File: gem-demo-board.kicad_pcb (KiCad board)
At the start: 6 copper layers, 56 x 66 mm, 153 parts, among them J1 3220-10-0100-00, J10 0473460001, J2 DF13A-2P-1.25H, J3 3220-10-0100-00, J4 2x20_Header_Female, J5 0473460001, J6 556500488, J7 556500488, J8 WE_686115148922_FLIPPED, J9 WE_686115148922_FLIPPED, U1 MCP1700T-3302E_TT, U2 NTS0104BQ, U3 NTS0104BQ, U4 NTS0104BQ, U5 93LC56CT-IMC, U6 FT4232HQ, U7 NTB0104BQ, U8 NTB0104BQ, Y1 ASFLMB-12.000MHZ-LC-T

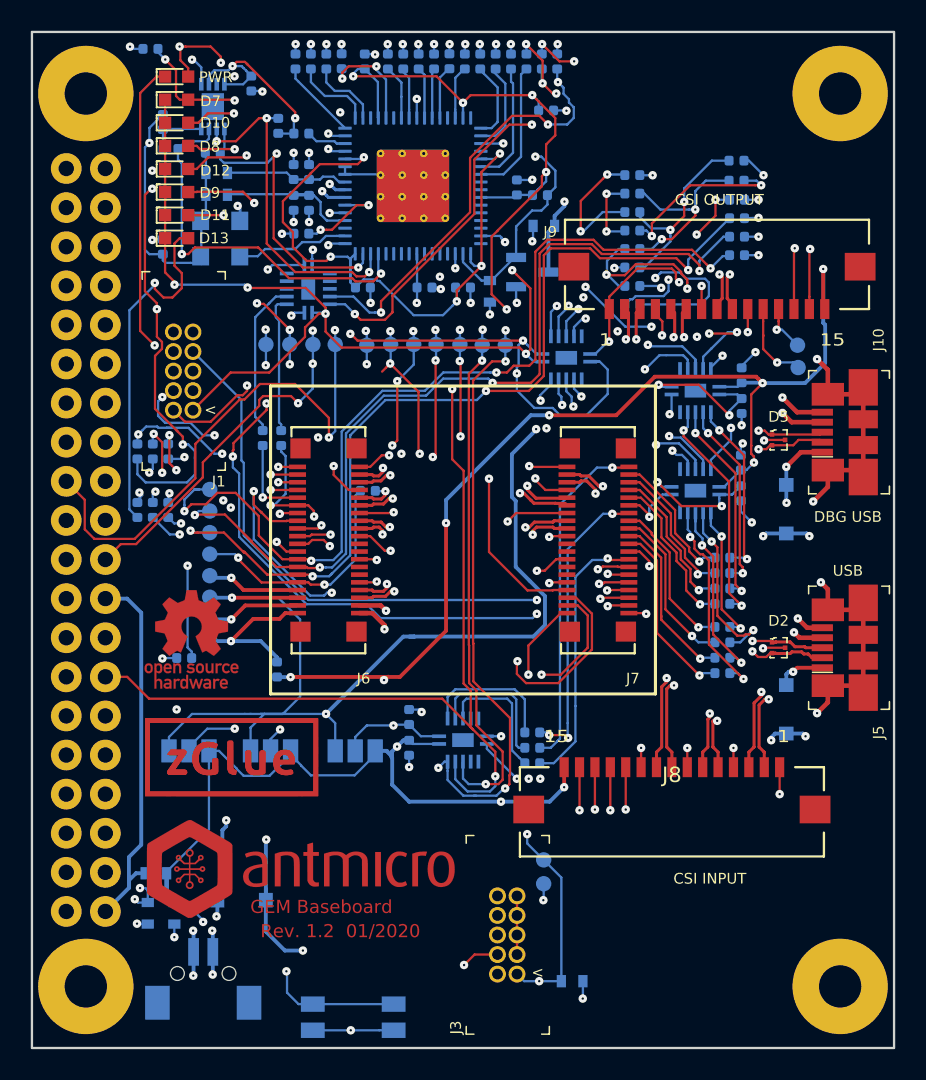
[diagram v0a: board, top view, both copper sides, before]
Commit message: Moved JTAG connector
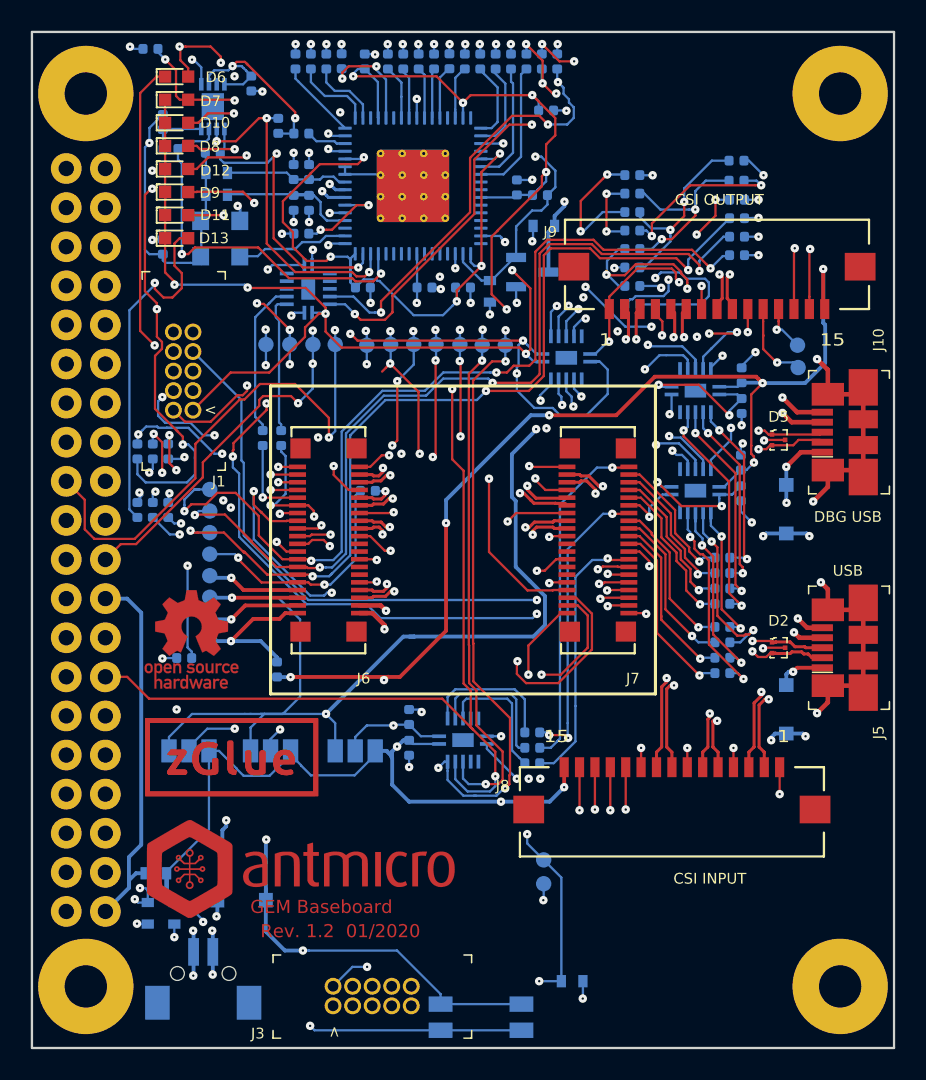
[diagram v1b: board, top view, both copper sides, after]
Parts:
- C1, C2, C3, C4, C5: footprint zglue-demo-board-footprints:0603-cap -> gem-demo-board-footprints:0603-cap
- C10, C11, C12, C13, C14, C15, C16, C17, C18, C19, C20, C21, C22, C23, C24, C25, C26, C9: footprint zglue-demo-board-footprints:0402-cap -> gem-demo-board-footprints:0402-cap
- D1, D3, D4: footprint zglue-demo-board-footprints:SOD-123 -> gem-demo-board-footprints:SOD-123
- D10, D11, D12, D13, D7, D8, D9: footprint zglue-demo-board-footprints:LED_0603 -> gem-demo-board-footprints:LED_0603
- D2, D5: footprint zglue-demo-board-footprints:SOT-3 -> gem-demo-board-footprints:SOT-3
- D6: renamed from PWR; footprint zglue-demo-board-footprints:LED_0603 -> gem-demo-board-footprints:LED_0603
- FB1, FB2, R1: footprint zglue-demo-board-footprints:0603-res -> gem-demo-board-footprints:0603-res
- J1, J3: footprint zglue-demo-board-footprints:PinHeader_2x5_P1.27mm_Drill.7mm -> gem-demo-board-footprints:PinHeader_2x5_P1.27mm_Drill.7mm
- J10, J5: footprint zglue-demo-board-footprints:USB_Micro_B_Female_0473460001 -> gem-demo-board-footprints:USB_Micro_B_Female_0473460001
- J2: footprint zglue-demo-board-footprints:DF13A-2P-1.25H -> gem-demo-board-footprints:DF13A-2P-1.25H
- J4: footprint zglue-demo-board-footprints:PinHeader_2x40_P2.54_Drill1mm -> gem-demo-board-footprints:PinHeader_2x40_P2.54_Drill1mm
- J6, J7: footprint zglue-demo-board-footprints:556500488 -> gem-demo-board-footprints:556500488
- J8, J9: footprint zglue-demo-board-footprints:WE_686115148922_FLIPPED -> gem-demo-board-footprints:WE_686115148922_FLIPPED
- N1: footprint zglue-demo-board-footprints:antmicro-logo_scaled_20mm -> gem-demo-board-footprints:antmicro-logo_scaled_20mm
- N2: footprint zglue-demo-board-footprints:zglue-logo-10000dpi -> gem-demo-board-footprints:zglue-logo-10000dpi
- N2: footprint zglue-demo-board-footprints:zglue-logo -> gem-demo-board-footprints:zglue-logo
- N3: footprint zglue-demo-board-footprints:oshw-logo -> gem-demo-board-footprints:oshw-logo
- R10, R11, R12, R13, R14, R15, R16, R17, R18, R19, R2, R20, R21, R22, R23, R24, R25, R26, R27, R28, R29, R3, R30, R31, R32, R33, R34, R35, R36, R37, R38, R39, R4, R40, R41, R42, R43, R44, R45, R46, R47, R48, R49, R5, R50, R51, R52, R53, R54, R55, R56, R57, R6, R60, R7, R8, R9: footprint zglue-demo-board-footprints:0402-res -> gem-demo-board-footprints:0402-res
- REF** (x4): footprint zglue-demo-board-footprints:Mount-hole-M2.5 -> gem-demo-board-footprints:Mount-hole-M2.5
- S1: footprint zglue-demo-board-footprints:Panasonic_EVQPUJ_EVQPUA -> gem-demo-board-footprints:Panasonic_EVQPUJ_EVQPUA
- TP1, TP10, TP11, TP12, TP13, TP14, TP15, TP16, TP17, TP18, TP19, TP2, TP20, TP21, TP22, TP23, TP3, TP4, TP5, TP6, TP7, TP8, TP9: footprint zglue-demo-board-footprints:Testpoint_smd_1mm -> gem-demo-board-footprints:Testpoint_smd_1mm
- U1: footprint zglue-demo-board-footprints:SOT-23-3 -> gem-demo-board-footprints:SOT-23-3
- U2, U3, U4, U7, U8: footprint zglue-demo-board-footprints:QDHVQFN14 -> gem-demo-board-footprints:QDHVQFN14
- U5: footprint zglue-demo-board-footprints:DFN-8_2x3mm -> gem-demo-board-footprints:DFN-8_2x3mm
- U6: footprint zglue-demo-board-footprints:FT4232HQ -> gem-demo-board-footprints:FT4232HQ
- Y1: footprint zglue-demo-board-footprints:ASFLMB -> gem-demo-board-footprints:ASFLMB
- moved J3 12.1 mm to (47.4, 93.5), turned to 0 degrees
- moved S1 8.30 mm to (57.0, 94.2)
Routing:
- net /PWR_BTN: track 48.7 -> 68.9 mm
- net /TDO: track 42.8 -> 53.4 mm
- net /3V3_SYS: track 227.7 -> 237.1 mm
- net /VUSB: track 78.3 -> 85.6 mm, vias 10 -> 9
- net /TDI: track 40.7 -> 47.8 mm
- net /TMS: track 42.2 -> 48.7 mm, vias 1 -> 2
- net /TCK: track 43.5 -> 47.7 mm, vias 2 -> 1
- net GND: track 179.8 -> 178.5 mm

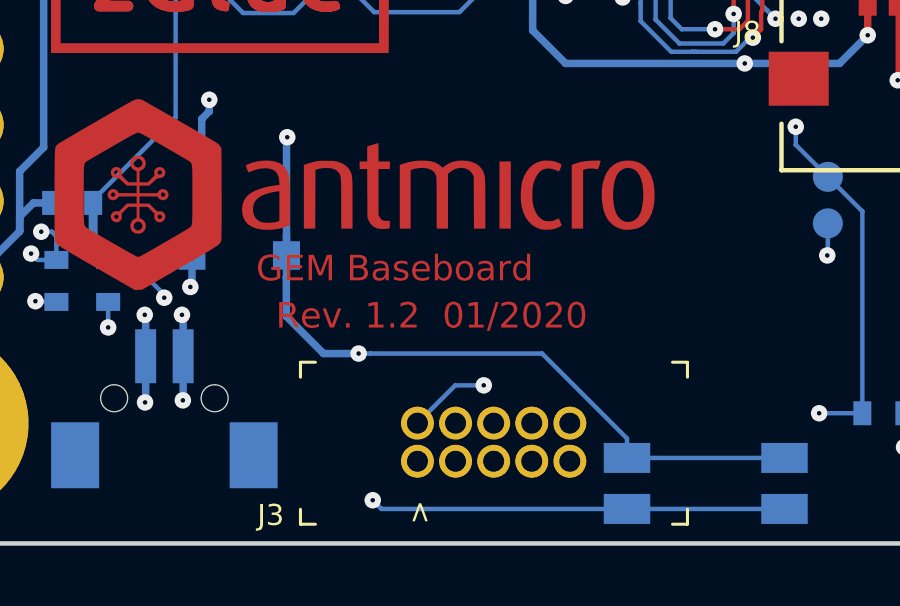
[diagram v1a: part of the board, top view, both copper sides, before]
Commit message: Updated revision marking
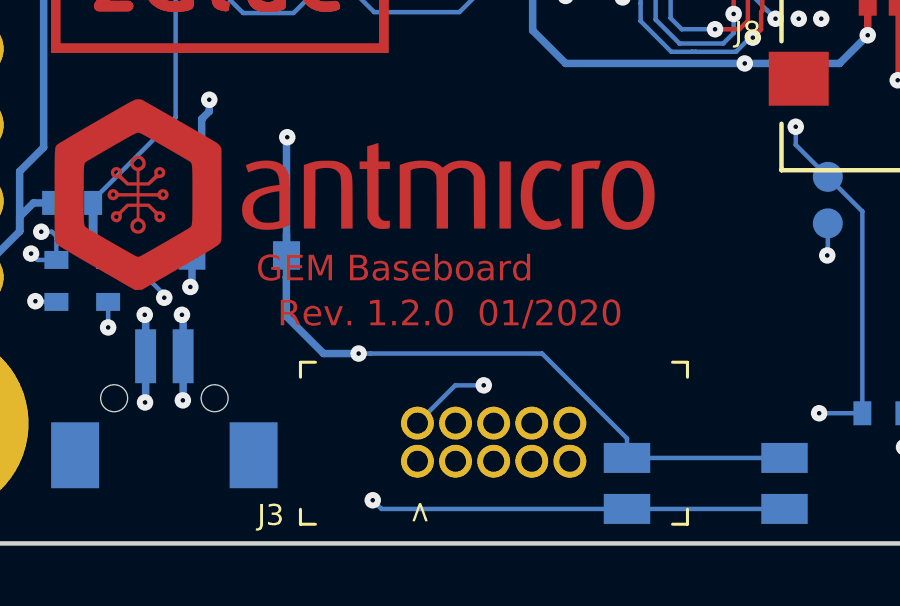
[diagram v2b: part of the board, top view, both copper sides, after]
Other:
- board text added: "Rev. 1.2.0 01/2020"
- board text removed: "Rev. 1.2 01/2020"
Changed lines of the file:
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@@
     (36 B.SilkS user)
     (37 F.SilkS user)
-    (38 B.Mask user)
-    (39 F.Mask user hide)
+    (38 B.Mask user hide)
+    (39 F.Mask user)
     (40 Dwgs.User user hide)
     (41 Cmts.User user hide)
@@
   )
   (gr_line (start 27.8 96.25) (end 83.8 96.25) (layer Edge.Cuts) (width 0.15))
-  (gr_text "Rev. 1.2  01/2020" (at 47.835 88.66) (layer F.Mask)
+  (gr_text "Rev. 1.2.0  01/2020" (at 48.445 88.585) (layer F.Mask)
     (effects (font (size 0.85 0.85) (thickness 0.18)))
   )
@@
     (effects (font (size 0.85 0.85) (thickness 0.18)))
   )
-  (gr_text "Rev. 1.2  01/2020" (at 47.835 88.66) (layer F.Cu)
+  (gr_text "Rev. 1.2.0  01/2020" (at 48.445 88.585) (layer F.Cu)
     (effects (font (size 0.85 0.85) (thickness 0.18)))
   )
